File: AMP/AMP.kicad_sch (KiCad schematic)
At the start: 147 parts, among them J1 AudioJack4, J2 AudioJack4, J3 Screw_Terminal_01x02, J4 Barrel_Jack_MountingPin, U1 NE5532, U10 NE5532, U11 NE5532, U13 NE5532, U14 NE5532, U15 NE5532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

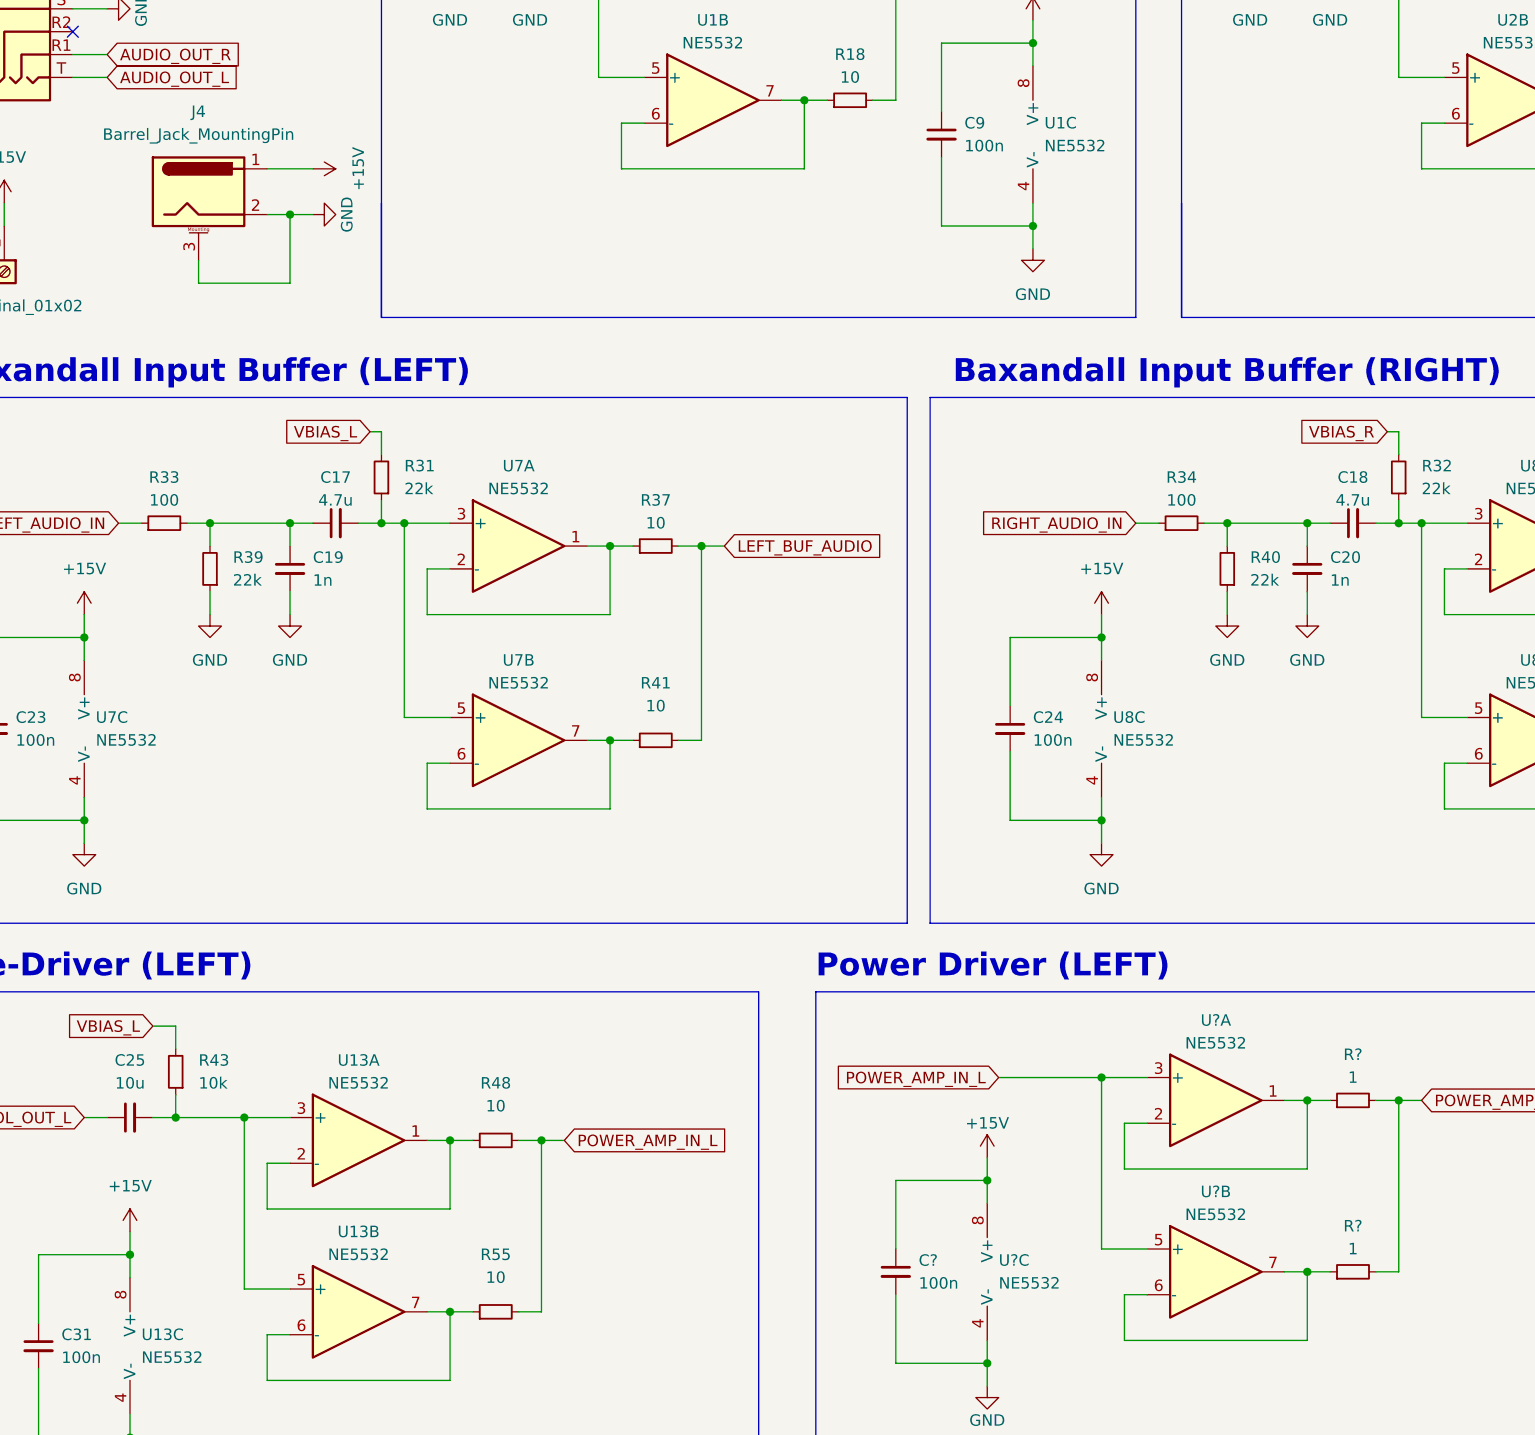
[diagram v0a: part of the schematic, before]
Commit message: Updated AMP PCB
- added silkscreen
- added cad models for 3d view
- convert to kicad 7.0
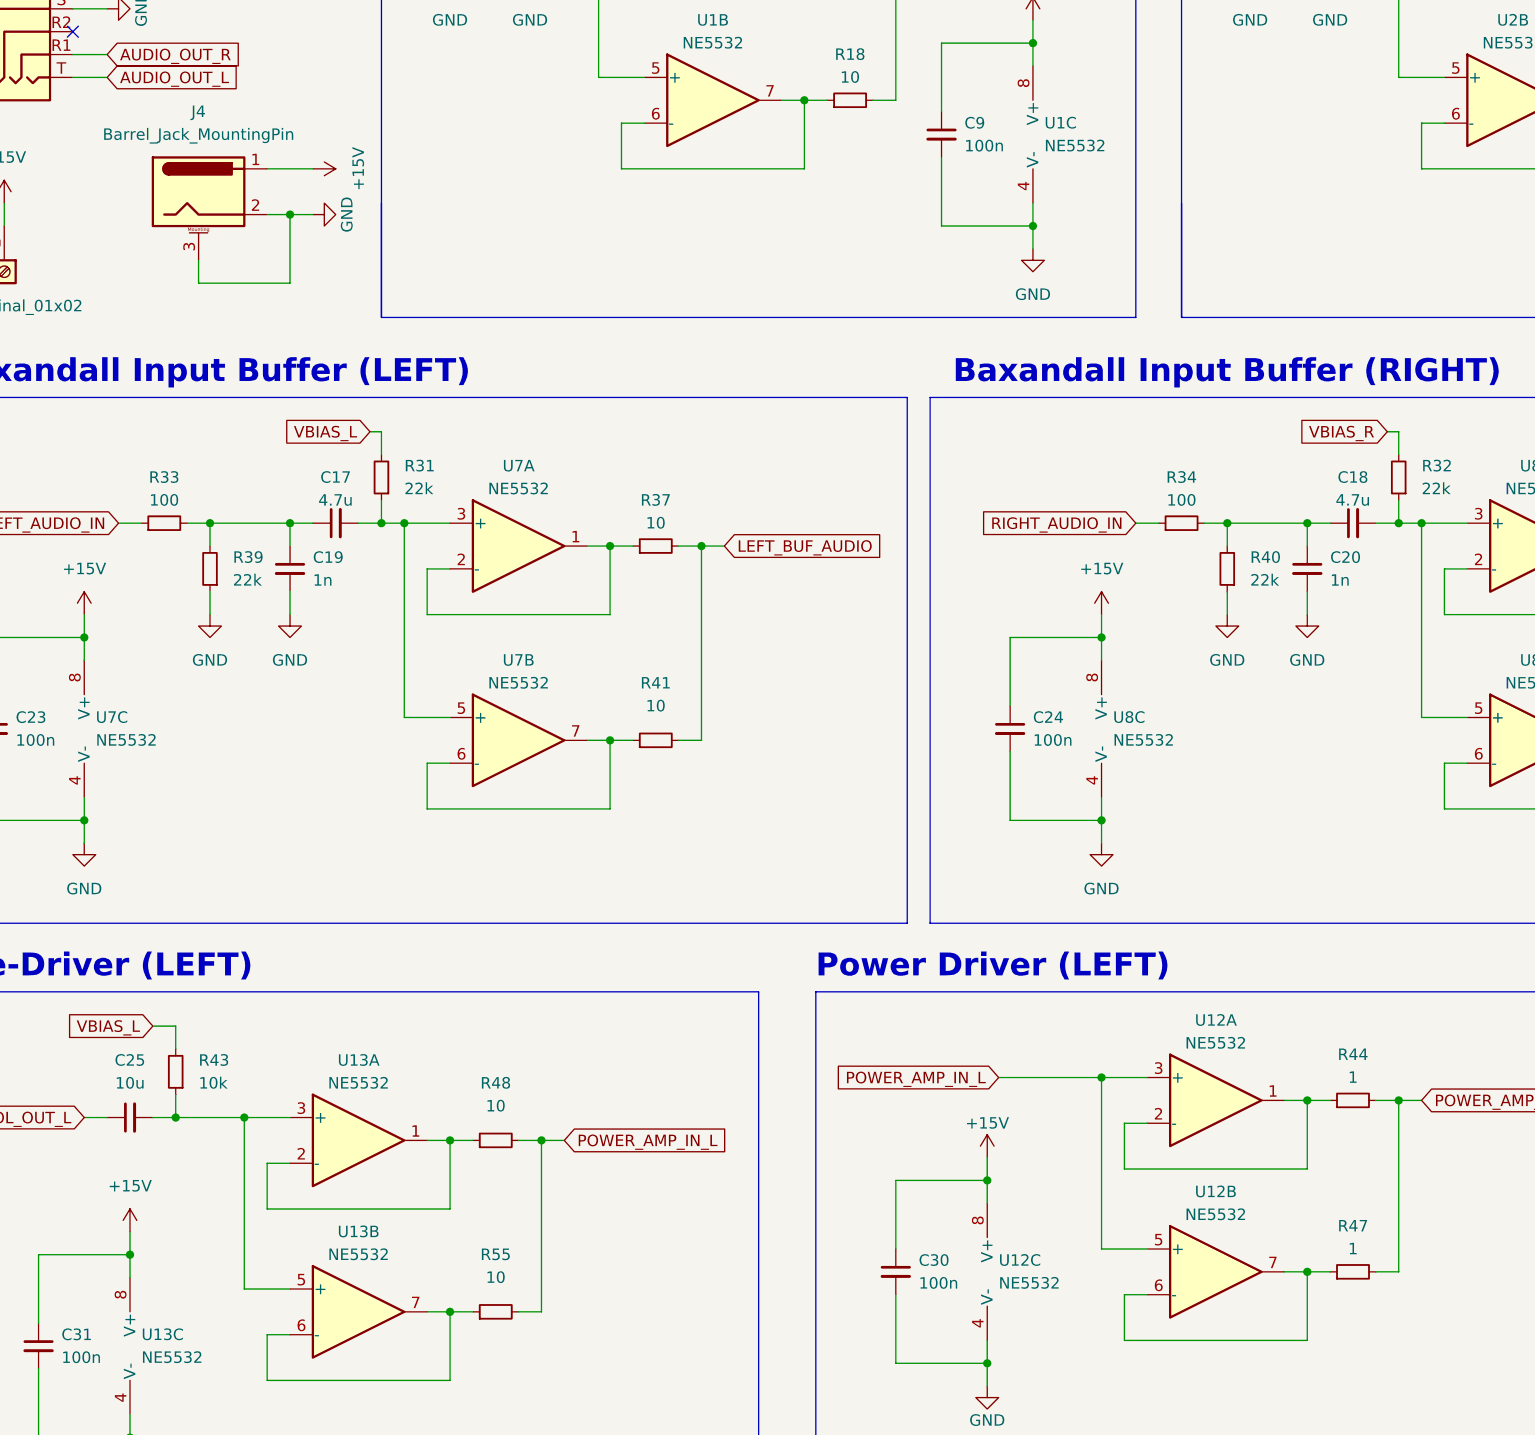
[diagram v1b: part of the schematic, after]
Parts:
- gave numbers to parts that had none: 4
